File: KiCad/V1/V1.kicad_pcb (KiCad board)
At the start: 4 copper layers, 130.8 x 93.1 mm, 59 parts, among them Q1 Q_NMOS_GSD, Q2 Q_NMOS_GSD, U1 LMG1210RVRR, U2 OPA2677IDDA, U3 OPA2677IDDA, U4 OPA859QDSGRQ1, U5 OPA859QDSGRQ1

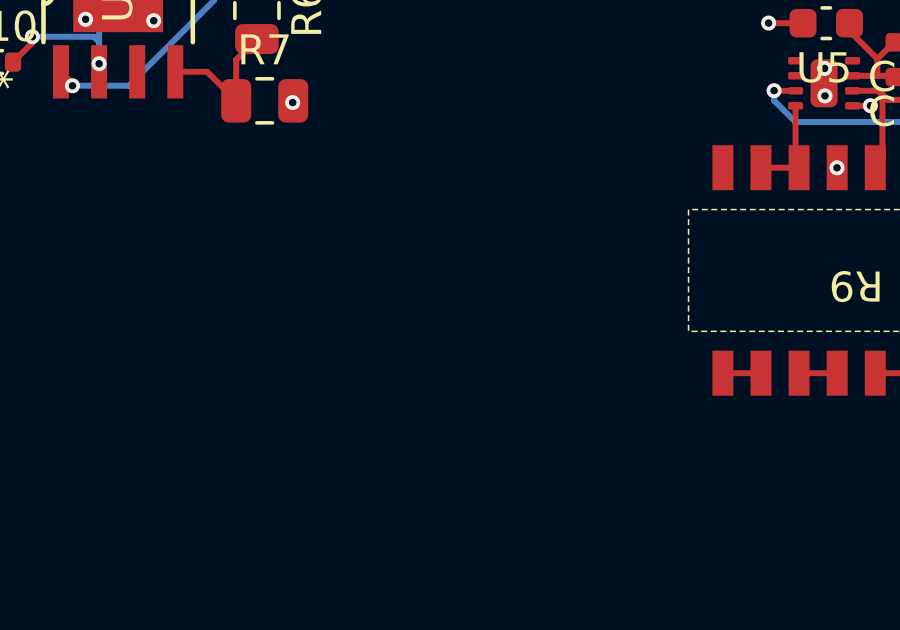
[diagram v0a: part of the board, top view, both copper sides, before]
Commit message: added integrator
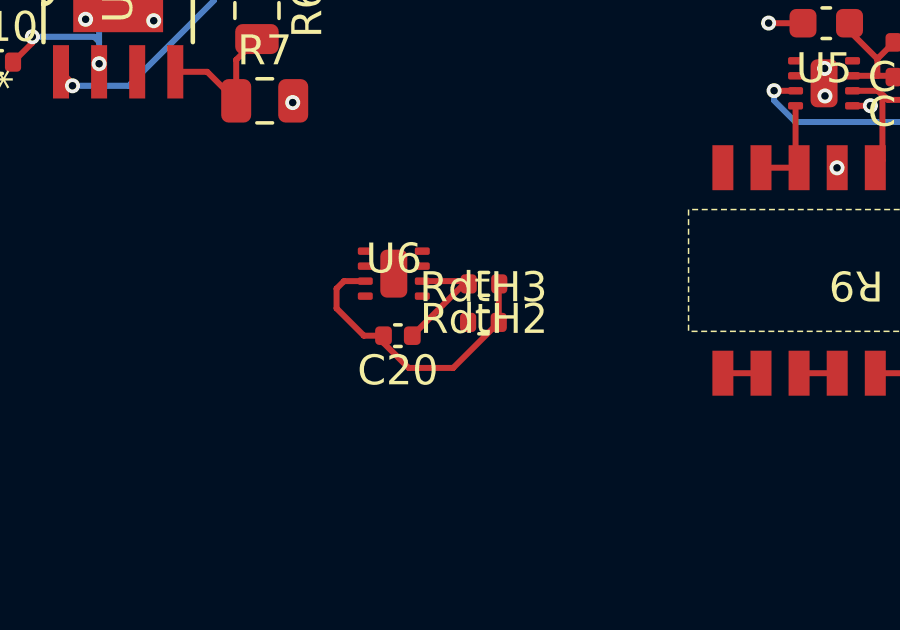
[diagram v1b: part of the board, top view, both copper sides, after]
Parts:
- added C20: 30p, Capacitor_SMD:C_0402_1005Metric, F.Cu at (122.1, 65.6)
- added RdtH2: 10k, Resistor_SMD:R_0402_1005Metric, F.Cu at (125.0, 63.9)
- added RdtH3: 10k, Resistor_SMD:R_0402_1005Metric, F.Cu at (125.0, 65.2)
- added U6: OPA859QDSGRQ1, MyFootprints:OPA859QDSGRQ1, F.Cu at (122.0, 63.6)
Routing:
- net Net-(U6-IN-): track 0.00 -> 10.0 mm
- net Net-(U6-OUT): track 0.00 -> 4.18 mm

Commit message: eddit
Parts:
- removed R10: 150, Resistor_SMD:R_0402_1005Metric
- removed R7: 0, Capacitor_SMD:C_0805_2012Metric
- added C21: 10u, Capacitor_SMD:C_0402_1005Metric, F.Cu at (126.7, 62.2)
- added C22: 1u, Capacitor_SMD:C_0402_1005Metric, F.Cu at (125.4, 62.2)
- added C23: 10n, Capacitor_SMD:C_0402_1005Metric, F.Cu at (124.2, 62.3)
- added R3: 0, Capacitor_SMD:C_0805_2012Metric, F.Cu at (119.8, 55.1)
- R1, R12, R14: value 47 -> 49.9
- moved R6 0.24 mm to (117.4, 55.0)
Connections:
- C10 pad 2: +5V -> +2V
- C13 pad 2: /-Shunt -> /OUT
- C16 pad 2: +5V -> +2V
- C18 pad 2: VPWN_Gen -> 2V
- C2 pad 2: VPWN_Gen -> 2V
- C20 pad 1: Net-(U6-OUT) -> /V_sens
- C5 pad 2: VPWN_Gen -> 2V
- C9 pad 2: +5V -> +2V
- L2 pad 2: /+Shunt -> Net-(L2-Pad2)
- R6 pad 1: -1V -> Net-(U3-VS-)
- R6 pad 2: Net-(U3-VS-) -> GND
- R8 pad 1: /-Shunt -> Net-(L2-Pad2)
- R8 pad 4: /V_sens -> Net-(U4-OUT)
- R8 pad 8: /+Shunt -> /OUT
- RV1 pad 2: Net-(R10-Pad1) -> Net-(U2-OUTB)
- R_shutn1 pad 1: /+Shunt -> Net-(L2-Pad2)
- R_shutn1 pad 2: /-Shunt -> /OUT
- RdtH2 pad 2: Net-(U6-OUT) -> /V_sens
- RdtH3 pad 1: /V_sens -> Net-(U4-OUT)
- U2 pad 2: VPWN_Gen/2 -> GND
- U2 pad 4: GND -> -2V
- U2 pad 8: VPWN_Gen -> 2V
- U3 pad 7: VPWN_Gen -> +5V
- U4 pad 6: /V_sens -> Net-(U4-OUT)
- U5 pad 5: GND -> -2V
- U5 pad 7: +5V -> +2V
- U6 pad 6: Net-(U6-OUT) -> /V_sens
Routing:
- net (no net): track 0.00 -> 31.7 mm
- net VPWN_Gen: track 15.7 -> 0.00 mm, vias 2 -> 0
- net /-Shunt: track 9.71 -> 0.00 mm
- net /+Shunt: track 6.25 -> 0.00 mm
- net +2V: track 0.00 -> 4.70 mm
- net Net-(U6-OUT): track 4.18 -> 0.00 mm
- net Net-(U4-OUT): track 0.00 -> 2.78 mm
- net Net-(R10-Pad1): track 2.59 -> 0.00 mm
- net Net-(U2-OUTB): track 21.7 -> 24.3 mm
- net Net-(U3-VS-): track 4.78 -> 6.31 mm
- net /V_sens: track 2.78 -> 4.18 mm
- net +5V: track 10.0 -> 9.11 mm, vias 0 -> 2
- net GND: track 21.0 -> 20.3 mm, vias 55 -> 53
- net -2V: track 0.00 -> 0.60 mm, vias 0 -> 1

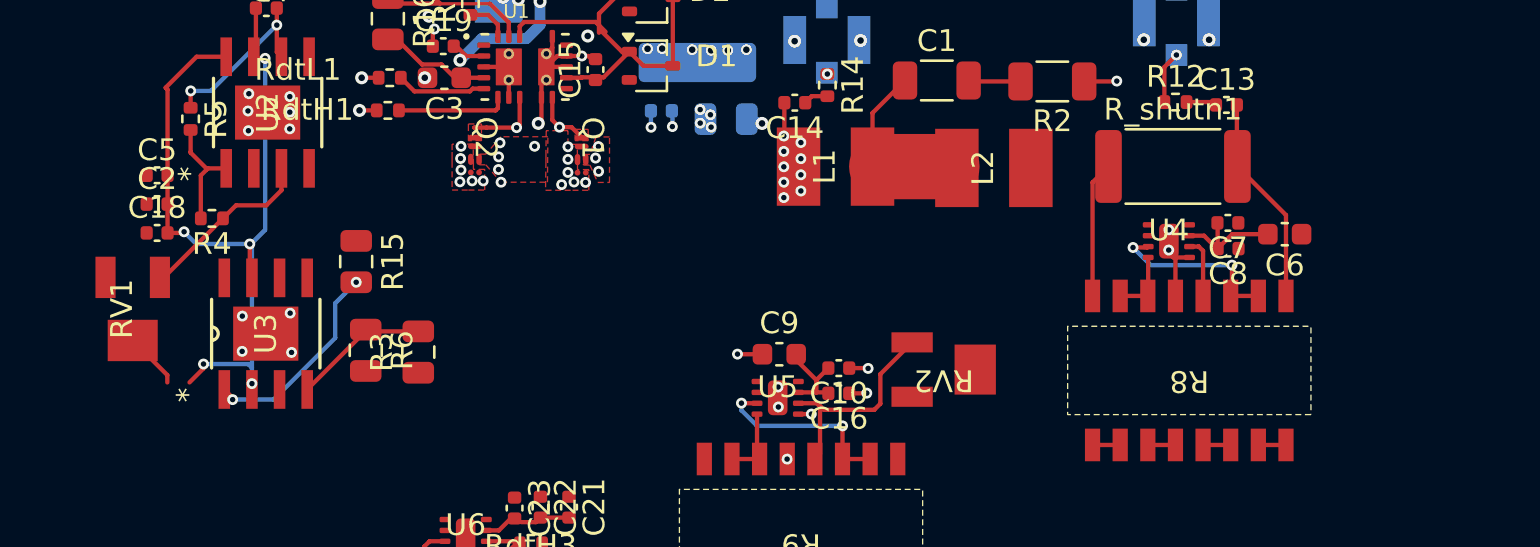
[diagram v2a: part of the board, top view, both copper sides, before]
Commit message: added integrator
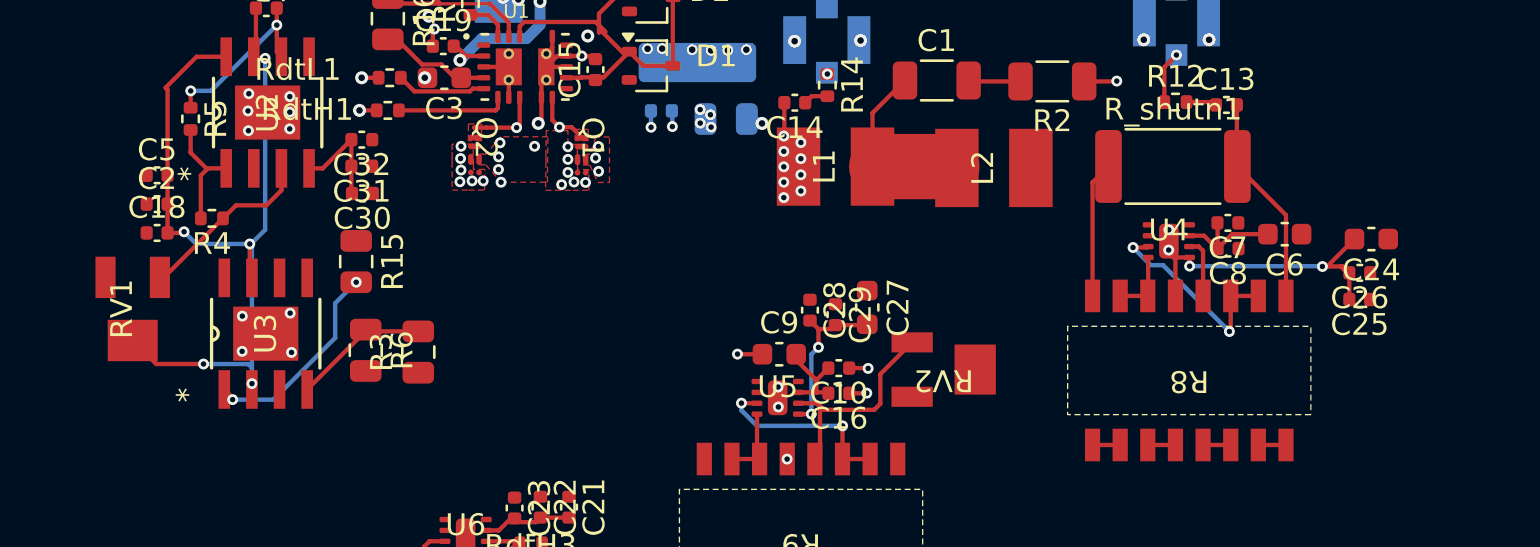
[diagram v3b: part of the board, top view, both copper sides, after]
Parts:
- added C24: 10u, Capacitor_SMD:C_0603_1608Metric, F.Cu at (163.6, 49.9)
- added C25: 1u, Capacitor_SMD:C_0402_1005Metric, F.Cu at (163.1, 52.7)
- added C26: 10n, Capacitor_SMD:C_0402_1005Metric, F.Cu at (163.1, 51.5)
- added C27: 10u, Capacitor_SMD:C_0603_1608Metric, F.Cu at (140.4, 53.1)
- added C28: 1u, Capacitor_SMD:C_0402_1005Metric, F.Cu at (137.8, 53.2)
- added C29: 10n, Capacitor_SMD:C_0402_1005Metric, F.Cu at (139.0, 53.4)
- added C30: 10u, Capacitor_SMD:C_0402_1005Metric, F.Cu at (117.2, 47.8)
- added C31: 1u, Capacitor_SMD:C_0402_1005Metric, F.Cu at (117.2, 46.6)
- added C32: 10n, Capacitor_SMD:C_0402_1005Metric, F.Cu at (117.2, 45.3)
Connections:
- C6 pad 2: +5V -> +2V
- C7 pad 2: +5V -> +2V
- C8 pad 2: +5V -> +2V
- L2 pad 2: Net-(L2-Pad2) -> Net-(T1-AA)
- R8 pad 1: Net-(L2-Pad2) -> Net-(T1-SA)
- R8 pad 8: /OUT -> Net-(T1-SB)
- R_shutn1 pad 1: Net-(L2-Pad2) -> Net-(T1-SB)
- R_shutn1 pad 2: /OUT -> Net-(T1-SA)
- U4 pad 5: GND -> -2V
- U4 pad 7: +5V -> +2V
- U6 pad 5: -5V -> -2V
- U6 pad 7: +5V -> +2V
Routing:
- net -2V: track 0.60 -> 24.1 mm, vias 1 -> 4
- net (no net): track 31.7 -> 25.4 mm
- net Net-(T1-SB): track 0.00 -> 6.25 mm
- net +2V: track 4.70 -> 10.0 mm
- net +5V: track 9.11 -> 3.80 mm
- net Net-(U4-IN-): track 8.30 -> 9.67 mm

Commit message: V1 pcb almost done
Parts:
- removed RdtH2, RdtH3: 10k, Resistor_SMD:R_0402_1005Metric
- added Pre_Filter2: Conn_Coaxial, Connector_Coaxial:U.FL_Molex_MCRF_73412-0110_Vertical, B.Cu at (118.3, 61.6)
- added Pre_Filter3: Conn_Coaxial, Connector_Coaxial:U.FL_Molex_MCRF_73412-0110_Vertical, B.Cu at (132.0, 61.6)
- added Pre_Filter4: Conn_Coaxial, Connector_Coaxial:U.FL_Molex_MCRF_73412-0110_Vertical, B.Cu at (125.6, 61.6)
- added R10: 150, Resistor_SMD:R_0402_1005Metric, F.Cu at (128.1, 54.9)
- added R11: 10k, Resistor_SMD:R_0402_1005Metric, F.Cu at (124.8, 50.1)
- added R13: 150, Resistor_SMD:R_0402_1005Metric, F.Cu at (109.0, 56.8)
- added R7: 150, Resistor_SMD:R_0402_1005Metric, F.Cu at (122.9, 54.9)
- added VDD2: MountingHole_Pad, TestPoint:TestPoint_THTPad_D2.5mm_Drill1.2mm, F.Cu at (103.7, 24.4)
- added VDD3: MountingHole_Pad, TestPoint:TestPoint_THTPad_D2.5mm_Drill1.2mm, F.Cu at (109.1, 24.4)
- added VDD4: MountingHole_Pad, TestPoint:TestPoint_THTPad_D2.5mm_Drill1.2mm, F.Cu at (114.6, 24.4)
- added VDD_PWM_BIG2: MountingHole_Pad, MountingHole:MountingHole_2.5mm_Pad_TopBottom, F.Cu at (166.4, 46.5)
- added VDD_PWM_BIG3: MountingHole_Pad, MountingHole:MountingHole_2.5mm_Pad_TopBottom, F.Cu at (166.4, 56.3)
- C14, L1, L2, R14: moved to B.Cu
- R8, R9: footprint MyFootprints:TOMCT16031002ZT1 -> MyFootprints:NOMCT16031
- R_shutn1: footprint Resistor_SMD:R_2512_6332Metric -> Resistor_SMD:R_1020_2550Metric_Pad1.33x5.20mm_HandSolder
- moved R12 40.9 mm to (133.5, 78.7)
- moved C13 40.9 mm to (135.8, 78.8)
- moved Post_Filter1 40.9 mm to (133.5, 75.0)
- moved PWM_IN1 26.3 mm to (111.8, 61.6), turned to -90 degrees
- moved R1 23.6 mm to (113.4, 61.0), turned to -90 degrees
- moved Pre_Filter1 20.8 mm to (138.3, 61.5), turned to 0 degrees
- moved R14 14.7 mm to (139.0, 57.5), turned to 90 degrees
- moved C14 12.2 mm to (139.0, 55.7), turned to 90 degrees
- moved C25 11.0 mm to (156.2, 61.2)
- moved U4 11.0 mm to (147.4, 58.5)
- moved C26 11.0 mm to (156.2, 60.0)
- moved C6 11.0 mm to (152.7, 58.2)
- moved C24 11.0 mm to (156.7, 58.4)
- moved C7 11.0 mm to (150.1, 57.7)
- moved C8 11.0 mm to (150.1, 58.9)
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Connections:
- net Net-(U4-OUT) renamed /V_diffsense
- C18 pad 2: 2V -> +2V
- C2 pad 2: 2V -> +2V
- C5 pad 2: 2V -> +2V
- U2 pad 8: 2V -> +2V
- U3 pad 2: Net-(U2-OUTB) -> Net-(U3-INA-)
- U3 pad 5: unconnected-(U3-INB+-Pad5) -> GND
- U3 pad 6: unconnected-(U3-INB--Pad6) -> Net-(U3-INB-)
- U3 pad 7: +5V -> Net-(U3-INB-)
- U3 pad 8: -VPWM_comp -> +5V
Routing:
- net +2V: track 10.0 -> 115.7 mm, vias 0 -> 5
- net -2V: track 24.1 -> 101.9 mm, vias 4 -> 8
- net +5V: track 3.80 -> 49.1 mm
- net /V_Error: track 0.00 -> 38.0 mm
- net /V_diffsense: track 2.78 -> 37.9 mm, vias 0 -> 2
- net Net-(U1-PWM/LI): track 1.99 -> 28.7 mm, vias 0 -> 4
- net (no net): track 25.4 -> 0.00 mm
- net /EN1: track 21.4 -> 44.0 mm, vias 0 -> 5
- net Net-(T1-AA): track 0.00 -> 17.5 mm
- net /V_sens: track 4.18 -> 21.3 mm, vias 0 -> 2
- net Net-(T1-SA): track 0.00 -> 8.17 mm
- net /HS1: track 9.62 -> 17.7 mm, vias 21 -> 22
- net Net-(U3-INA-): track 0.00 -> 5.43 mm
- net Net-(T1-SB): track 6.25 -> 10.2 mm
- net /Pre_Filter1: track 0.07 -> 2.29 mm, vias 1 -> 0
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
